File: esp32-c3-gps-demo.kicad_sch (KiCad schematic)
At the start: 41 parts, among them J1 USB_C_Receptacle_USB2.0_16P, Q1 HL3407A, U1 TPS54331, U10 TPS613222ADBV, U3 SRV05-4, U8 AP2112K-3.3, U9 BQ24073RGT

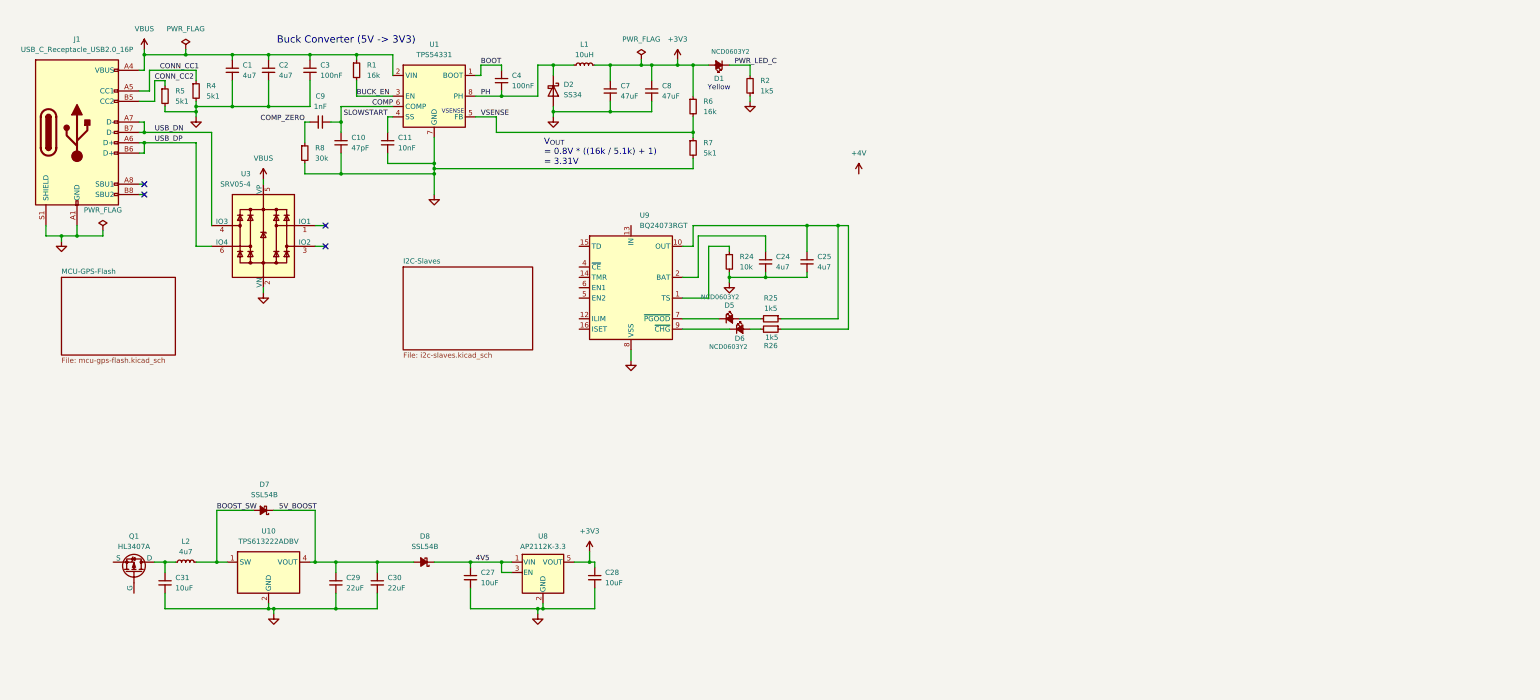
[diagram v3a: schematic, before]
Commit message: Added ORing circuit for USB 5V and boost converter 5V
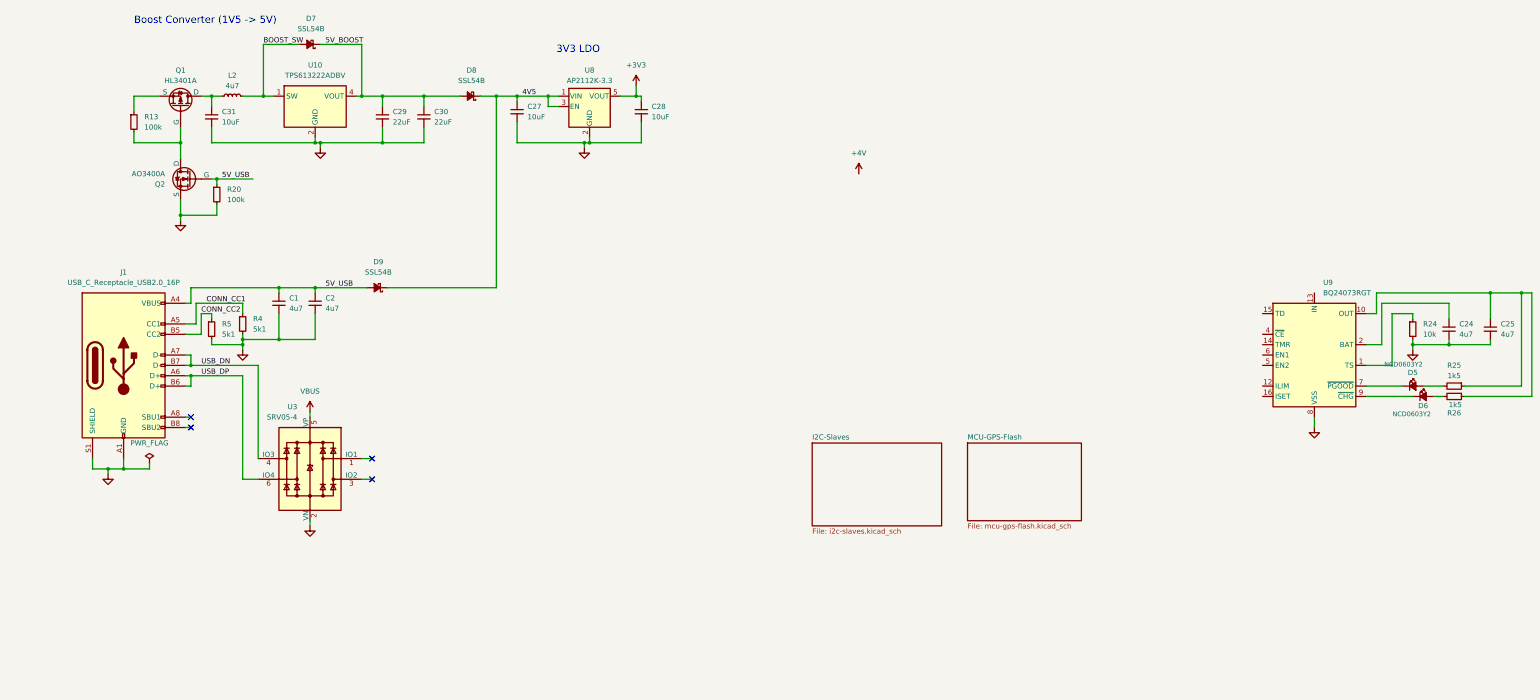
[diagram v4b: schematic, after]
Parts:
- removed C10: 47pF, Capacitor_SMD:C_0603_1608Metric, symbol Device:C_Small
- removed C11: 10nF, Capacitor_SMD:C_0603_1608Metric, symbol Device:C_Small
- removed C3, C4: 100nF, Capacitor_SMD:C_0603_1608Metric, symbol Device:C_Small
- removed C7, C8: 47uF, Capacitor_SMD:C_0805_2012Metric, symbol Device:C_Small
- removed C9: 1nF, Capacitor_SMD:C_0603_1608Metric, symbol Device:C_Small
- removed D1: NCD0603Y2, LED_SMD:LED_0603_1608Metric, symbol Device:LED_Small_Filled
- removed D2: SS34, Diode_SMD:D_SMA, symbol Diode:SS34
- removed L1: 10uH, Inductor_SMD:L_Changjiang_FXL0630, symbol Device:L_Small
- removed R1, R6: 16k, Resistor_SMD:R_0805_2012Metric, symbol Device:R_Small
- removed R2: 1k5, Resistor_SMD:R_0603_1608Metric, symbol Device:R_Small
- removed R7: 5k1, Resistor_SMD:R_0603_1608Metric, symbol Device:R_Small
- removed R8: 30k, Resistor_SMD:R_0603_1608Metric, symbol Device:R_Small
- removed U1: TPS54331, Package_SO:SOIC-8_3.9x4.9mm_P1.27mm, symbol Regulator_Switching:TPS54233
- added D9: SSL54B, Diode_SMD:D_SMB, symbol Device:D_Schottky_Small_Filled
- added Q2: AO3400A, Package_TO_SOT_SMD:SOT-23, symbol Simulation_SPICE:NMOS
- added R13, R20: 100k, Resistor_SMD:R_0603_1608Metric, symbol Device:R_Small
- Q1: value HL3407A -> HL3401A; LCSC Part # C28646269 -> C7420349
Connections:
- net 4V5: now also D9.1 (K)
- net GND: now also Q2.3 (S), R20.2
- net VBUS: no longer C1.1, C2.1, J1.A4 (VBUS), J1.A9 (VBUS), J1.B4 (VBUS), J1.B9 (VBUS)
- net at Q1.2 (G): now also Q2.1 (D), R13.2
- net at Q1.3 (S): now also R13.1
- new net 5V_USB: C1.1, C2.1, D9.2 (A), J1.A4 (VBUS), J1.A9 (VBUS), J1.B4 (VBUS), J1.B9 (VBUS), Q2.2 (G), R20.1
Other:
- note added: "3V3 LDO"
- note added: "Boost Converter (1V5 -> 5V)"
- note removed: "Buck Converter (5V -> 3V3)"
- note removed: "VSENSE"
- note removed: "V_{OUT} = 0.8V * ((16k / 5.1k) + 1) = 3.31V"
- note removed: "Yellow"
- moved on the sheet: C1, C2, C24, C25, C27, C28, C29, C30, C31, D5, D6, D7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
